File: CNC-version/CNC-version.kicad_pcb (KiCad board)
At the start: 2 copper layers, 100 x 80 mm, 45 parts, among them J1 DIN-5_180degree, J2 DIN-5_180degree, J3 DIN-5_180degree, J4 DIN-5_180degree, J5 DIN-5_180degree, Q1 BC547, Q2 BC547, Q3 BC547, Q4 BC547, U1 6N138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

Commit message: Update of CNC-version
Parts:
- moved R15 3.81 mm to (63.5, 52.1)
- moved R16 3.81 mm to (67.3, 52.1)
- renumbered +5v1 to +5v, GND1 to GND, RXD1 to RXD, TXD1 to TXD
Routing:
- net Net-(U1-VO2): track 62.3 -> 53.4 mm
- removed copper zone on F.Cu, net GND
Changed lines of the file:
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@@
 	)
 	(paper "A4")
+	(title_block
+		(comment 4 "AISLER Project ID: TXHNPXDB")
+	)
 	(layers
 		(0 "F.Cu" signal)
@@
 		(tenting front back)
 		(pcbplotparams
-			(layerselection 0x00000000_00000000_55555555_55555554)
+			(layerselection 0x00000000_00000000_5555555f_5555ffff)
 			(plot_on_all_layers_selection 0x00000000_00000000_00000000_00000000)
 			(disableapertmacros no)
@@
 			(drillshape 0)
 			(scaleselection 1)
-			(outputdirectory "")
+			(outputdirectory "Gerber/")
 		)
 	)
@@
 		(descr "Soldered wire connection, for a single 1.5 mm² wire, reinforced insulation, conductor diameter 1.7mm, outer diameter 3.9mm, size source Multi-Contact FLEXI-xV 1.5 (https://www.staubli.com/content/dam/ecs/catalogs-brochures/TM/CAB-Main-11014119-en.pdf#page=11), bend radius 3 times outer diameter, generated with kicad-footprint-generator")
 		(tags "connector wire 1.5sqmm")
-		(property "Reference" "+5v1"
+		(property "Reference" "+5v"
 			(at 0 -3.15 0)
 			(layer "F.SilkS")
@@
 		(descr "Soldered wire connection, for a single 1.5 mm² wire, reinforced insulation, conductor diameter 1.7mm, outer diameter 3.9mm, size source Multi-Contact FLEXI-xV 1.5 (https://www.staubli.com/content/dam/ecs/catalogs-brochures/TM/CAB-Main-11014119-en.pdf#page=11), bend radius 3 times outer diameter, generated with kicad-footprint-generator")
 		(tags "connector wire 1.5sqmm")
-		(property "Reference" "TXD1"
+		(property "Reference" "TXD"
 			(at 0 -3.15 0)
 			(layer "F.SilkS")
@@
 		(descr "Soldered wire connection, for a single 1.5 mm² wire, reinforced insulation, conductor diameter 1.7mm, outer diameter 3.9mm, size source Multi-Contact FLEXI-xV 1.5 (https://www.staubli.com/content/dam/ecs/catalogs-brochures/TM/CAB-Main-11014119-en.pdf#page=11), bend radius 3 times outer diameter, generated with kicad-footprint-generator")
 		(tags "connector wire 1.5sqmm")
-		(property "Reference" "GND1"
+		(property "Reference" "GND"
 			(at 0 -3.15 0)
 			(layer "F.SilkS")
@@
 		(descr "Soldered wire connection, for a single 1.5 mm² wire, reinforced insulation, conductor diameter 1.7mm, outer diameter 3.9mm, size source Multi-Contact FLEXI-xV 1.5 (https://www.staubli.com/content/dam/ecs/catalogs-brochures/TM/CAB-Main-11014119-en.pdf#page=11), bend radius 3 times outer diameter, generated with kicad-footprint-generator")
 		(tags "connector wire 1.5sqmm")
-		(property "Reference" "RXD1"
+		(property "Reference" "RXD"
 			(at 0 -3.15 0)
 			(layer "F.SilkS")
@@
 	(footprint "PCM_Resistor_THT_AKL:R_Axial_DIN0207_L6.3mm_D2.5mm_P10.16mm_Horizontal"
 		(layer "F.Cu")
-		(at 63.5 52.06 90)
+		(at 67.31 52.06 90)
 		(descr "Resistor, Axial_DIN0207 series, Axial, Horizontal, pin pitch=10.16mm, 0.25W = 1/4W, length*diameter=6.3*2.5mm^2, http://cdn-reichelt.de/documents/datenblatt/B400/1_4W%23YAG.pdf, Alternate KiCad Library")
 		(tags "Resistor Axial_DIN0207 series Axial Horizontal pin pitch 10.16mm 0.25W = 1/4W length 6.3mm diameter 2.5mm")
@@
 	(footprint "PCM_Resistor_THT_AKL:R_Axial_DIN0207_L6.3mm_D2.5mm_P10.16mm_Horizontal"
 		(layer "F.Cu")
-		(at 67.31 52.06 90)
+		(at 63.5 52.07 90)
 		(descr "Resistor, Axial_DIN0207 series, Axial, Horizontal, pin pitch=10.16mm, 0.25W = 1/4W, length*diameter=6.3*2.5mm^2, http://cdn-reichelt.de/documents/datenblatt/B400/1_4W%23YAG.pdf, Alternate KiCad Library")
 		(tags "Resistor Axial_DIN0207 series Axial Horizontal pin pitch 10.16mm 0.25W = 1/4W length 6.3mm diameter 2.5mm")
@@
 	)
 	(segment
-		(start 63.5 52.06)
-		(end 67.31 52.06)
+		(start 67.31 58.41)
+		(end 63.5 58.41)
 		(width 1.27)
 		(layer "B.Cu")
@@
 	)
 	(segment
-		(start 67.31 58.41)
-		(end 63.5 58.41)
+		(start 67.31 52.06)
+		(end 63.51 52.06)
+		(width 1.27)
+		(layer "B.Cu")
+		(net 26)
+	)
+	(segment
+		(start 63.51 52.06)
+		(end 63.5 52.07)
 		(width 1.27)
 		(layer "B.Cu")
@@
 	)
 	(segment
-		(start 45.72 44.45)
-		(end 43.18 44.45)
-		(width 1.27)
-		(layer "B.Cu")
-		(net 29)
-	)
-	(segment
-		(start 33.02 44.44)
-		(end 40.64 44.44)
+		(start 52.08 39.37)
+		(end 55.88 39.37)
 		(width 1.27)
 		(layer "B.Cu")
@@
 	)
 	(segment
-		(start 60.96 39.36)
-		(end 60.96 44.45)
+		(start 45.72 44.45)
+		(end 43.18 44.45)
 		(width 1.27)
 		(layer "B.Cu")
@@
 	)
 	(segment
-		(start 55.88 39.37)
-		(end 52.08 39.37)
+		(start 33.02 44.44)
+		(end 40.64 44.44)
 		(width 1.27)
 		(layer "B.Cu")
@@
 	)
 	(segment
-		(start 55.87 39.38)
-		(end 55.88 39.37)
+		(start 55.88 44.45)
+		(end 63.5 44.45)
 		(width 1.27)
 		(layer "B.Cu")
@@
 	)
 	(segment
-		(start 52.08 39.37)
-		(end 52.07 39.36)
-		(width 1.27)
-		(layer "B.Cu")
-		(net 29)
-	)
-	(segment
-		(start 55.88 41.91)
-		(end 55.88 44.45)
+		(start 43.18 49.52)
+		(end 43.18 52.06)
 		(width 1.27)
 		(layer "B.Cu")
@@
 	)
 	(segment
-		(start 67.31 39.36)
-		(end 60.96 39.36)
+		(start 43.18 44.45)
+		(end 43.18 49.52)
 		(width 1.27)
 		(layer "B.Cu")
@@
 	)
 	(segment
-		(start 43.18 49.52)
-		(end 43.18 52.06)
+		(start 40.65 44.45)
+		(end 43.18 44.45)
 		(width 1.27)
 		(layer "B.Cu")
@@
 	)
 	(segment
-		(start 43.18 44.45)
-		(end 43.18 49.52)
+		(start 45.72 39.36)
+		(end 45.72 44.45)
 		(width 1.27)
 		(layer "B.Cu")
@@
 	)
 	(segment
-		(start 40.65 44.45)
-		(end 43.18 44.45)
+		(start 40.64 44.44)
+		(end 40.65 44.45)
 		(width 1.27)
 		(layer "B.Cu")
@@
 	)
 	(segment
-		(start 45.72 39.36)
-		(end 45.72 44.45)
+		(start 55.88 39.37)
+		(end 55.87 39.38)
 		(width 1.27)
 		(layer "B.Cu")
@@
 	)
 	(segment
-		(start 67.31 41.9)
-		(end 67.31 39.36)
+		(start 55.87 39.38)
+		(end 55.87 41.9)
 		(width 1.27)
 		(layer "B.Cu")
@@
 	)
 	(segment
-		(start 40.64 44.44)
-		(end 40.65 44.45)
+		(start 55.87 41.9)
+		(end 55.88 41.91)
 		(width 1.27)
 		(layer "B.Cu")
@@
 	)
 	(segment
-		(start 55.87 41.9)
-		(end 55.87 39.38)
+		(start 55.88 41.91)
+		(end 55.88 44.45)
 		(width 1.27)
 		(layer "B.Cu")
@@
 	)
 	(segment
-		(start 55.88 44.45)
-		(end 60.96 44.45)
+		(start 63.5 44.45)
+		(end 63.5 41.91)
 		(width 1.27)
 		(layer "B.Cu")
@@
 	)
 	(segment
-		(start 55.87 41.9)
-		(end 55.88 41.91)
+		(start 52.07 39.36)
+		(end 52.08 39.37)
 		(width 1.27)
 		(layer "B.Cu")
@@
 		(net 37)
 		(net_name "GND")
-		(layers "F.Cu" "B.Cu")
+		(layer "B.Cu")
 		(hatch edge 0.5)
 		(connect_pads

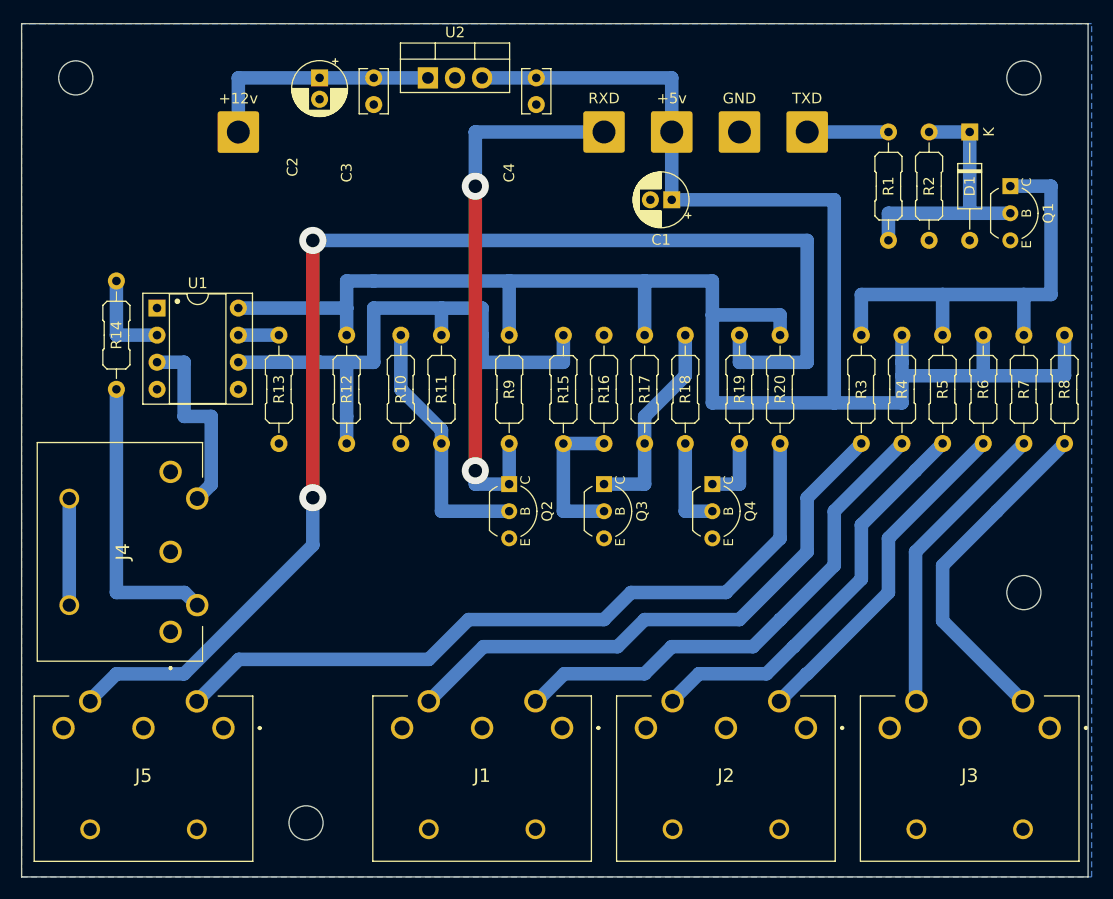
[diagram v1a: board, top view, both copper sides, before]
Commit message: Too close for comfort
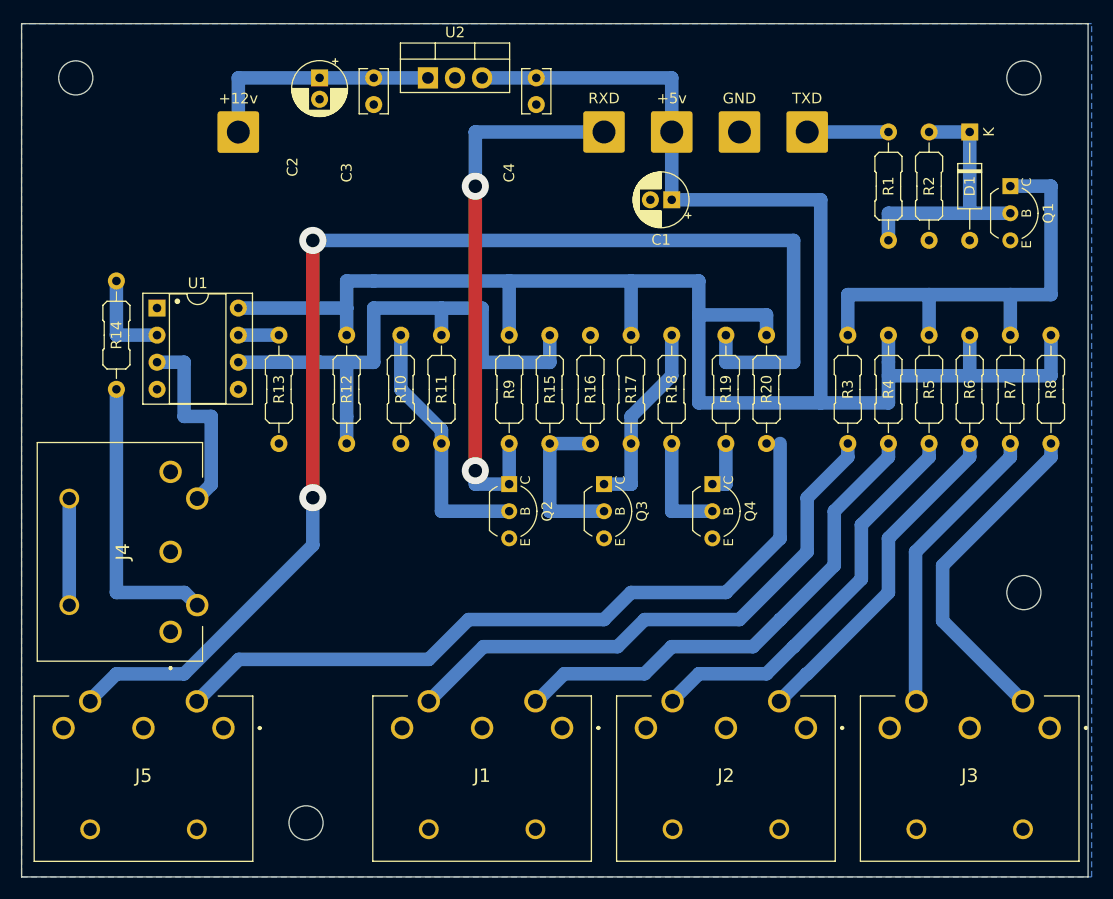
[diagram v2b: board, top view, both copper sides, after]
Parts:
- moved R17 1.27 mm to (69.8, 41.9)
- moved R16 1.27 mm to (66.0, 52.1)
- moved R18 1.27 mm to (73.7, 41.9)
- moved R19 1.27 mm to (78.7, 52.1)
- moved R6 1.27 mm to (101.6, 41.9)
- moved R7 1.27 mm to (105.4, 52.1)
- moved R15 1.27 mm to (62.2, 52.1)
- moved R20 1.27 mm to (82.5, 41.9)
- moved R3 1.27 mm to (90.2, 52.1)
- moved R4 1.27 mm to (94.0, 41.9)
- moved R5 1.27 mm to (97.8, 52.1)
- moved R8 1.27 mm to (109.2, 41.9)
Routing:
- net +5V: track 189.8 -> 187.3 mm
- net Net-(Q4-B): track 8.89 -> 10.2 mm
- net Net-(U1-VO2): track 53.4 -> 52.1 mm
- net Net-(Q3-B): track 14.0 -> 15.2 mm
- net Net-(J5-Pad5): track 122.3 -> 121.0 mm
- net Net-(Q4-C): track 6.35 -> 5.09 mm
- net Net-(Q3-C): track 19.4 -> 18.1 mm
- net Net-(Q1-C): track 43.2 -> 44.4 mm
- net Net-(J2-Pad4): track 32.1 -> 31.6 mm
- net Net-(J3-Pad5): track 28.4 -> 27.9 mm
- net Net-(J3-Pad4): track 32.0 -> 31.5 mm
- net Net-(J1-Pad4): track 47.4 -> 46.8 mm
- net Net-(J2-Pad5): track 38.4 -> 37.9 mm
- net Net-(J1-Pad5): track 53.5 -> 53.0 mm

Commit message: Even better layout
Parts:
- moved R10 10.2 mm to (48.3, 52.1), turned to 90 degrees
- moved R3 2.54 mm to (87.6, 52.1)
- moved R4 2.54 mm to (91.4, 41.9)
- moved R5 2.54 mm to (95.2, 52.1)
- moved R6 2.54 mm to (99.1, 41.9)
- moved R7 2.54 mm to (102.9, 52.1)
- moved R8 2.54 mm to (106.7, 41.9)
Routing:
- net +5V: track 187.3 -> 167.7 mm
- net Net-(J5-Pad5): track 121.0 -> 103.2 mm
- net Net-(Q2-B): track 24.4 -> 16.5 mm
- net Net-(Q1-C): track 44.4 -> 47.0 mm
- net Net-(J2-Pad5): track 37.9 -> 36.8 mm
- net Net-(J1-Pad5): track 53.0 -> 52.0 mm
- net Net-(J1-Pad4): track 46.8 -> 45.8 mm
- net Net-(J3-Pad5): track 27.9 -> 26.8 mm
- net Net-(J3-Pad4): track 31.5 -> 30.4 mm
- net Net-(J2-Pad4): track 31.6 -> 30.5 mm
- net Net-(J5-Pad4): track 69.9 -> 69.4 mm
